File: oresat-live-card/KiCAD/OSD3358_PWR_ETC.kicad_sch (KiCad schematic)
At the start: 35 parts, among them Q1 MMBT2907, U10 TLVH431, U18 RCLAMP0504FB, U4 SN74LVC1G07DCK, U7 OSD3358-512M-BSM

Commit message: Updated OreSat Live Card. Added changes from the C3 v6 Octavo circuitry and GPS card update. Fixed some GitHub issues. Board layout still in progress.
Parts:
- removed C41: 100n, Resistor_SMD:R_0603_1608Metric, symbol Device:C_Small
- removed JP101, JP104: JUMPER-SMT_2_NC_TRACE_SILK, Jumper:SolderJumper-2_P1.3mm_Bridged_RoundedPad1.0x1.5mm, symbol oresat-live-card-eagle-import:JUMPER-SMT_2_NC_TRACE_SILK
- removed R73, R74, R75: 100, Resistor_SMD:R_0603_1608Metric, symbol oresat-live-card-eagle-import:R-US_0603-A
- removed U18: RCLAMP0504FB, oresat-live-card:SC70-6, symbol oresat-live-card-eagle-import:RCLAMP0504FB
- added C33: 100n, Capacitor_SMD:C_0603_1608Metric, symbol Device:C_Small
- added D9 (x2): MBR0520L, Diode_SMD:D_SOD-123, symbol Device:D_Small
- added R48: 10k, Resistor_SMD:R_0603_1608Metric, symbol Device:R_Small_US
- D1: symbol oresat-live-card-eagle-import:LED-GREEN0603 -> Device:LED
- Q1: symbol oresat-live-card-eagle-import:MMBT2907SMD -> Device:Q_PNP_BEC
- R1: value 4.7k -> 10k; symbol oresat-live-card-eagle-import:R-US_0603-A -> oresat-passives:R-US
- R15, R23, R28, R31: symbol oresat-live-card-eagle-import:R-US_0603-A -> oresat-passives:R-US
- TP109, TP110, TP112, TP129, TP130, TP14, TP151, TP155, TP164, TP165, TP2, TP25, TP3, TP4, TP9: footprint oresat-live-card:PAD.03X.04 -> oresat-misc:TestPoint_Pad_D1.0mm; symbol oresat-live-card-eagle-import:TEST-POINT -> oresat-misc:Test-Point-1mm-round
- U10: symbol oresat-live-card-eagle-import:TLVH431 -> oresat-ics:TLVH431
- U4: symbol oresat-live-card-eagle-import:SN74LVC1G07DCK -> oresat-ics:SN74LVC1G07DCK
- U7: footprint oresat-live-card:OSD335X-BGA-256 -> oresat-ics:U-Octavo-OSD335X-BGA-256; symbol oresat-live-card-eagle-import:OSD3358-512M-BSM -> oresat-ics:OSD3358-512M-BSM
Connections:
- net 3.3V: now also D9.1 (K), D9.1 (K), R48.2; no longer U7.F6 (SYS_VDD1_3P3V@1), U7.F7 (SYS_VDD1_3P3V@2), U7.G6 (SYS_VDD1_3P3V@3), U7.G7 (SYS_VDD1_3P3V@4)
- net 3.3VA: now also Q1.2 (E), R23.2, R28.2
- net EEPROM_WP: now also U7.M2 (EEPROM_WP)
- net GND: now also D1.1 (K), C33.2; no longer D1.C
- net I2C0_SCL: now also U7.C10 (I2C0_SCL), U7.D10 (PMIC_SCL)
- net I2C0_SDA: now also U7.C11 (I2C0_SDA), U7.D11 (PMIC_SDA)
- net at R23.1, U10.2 (K): now also Q1.1 (B); no longer Q1.B
- net at R31.1, U10.3 (A): now also C18.1, Q1.3 (C), TP14.1, TP164.1, U4.5 (VCC), U7.K11 (SYS_RTC_1P8V@1), U7.L11 (SYS_RTC_1P8V@2); no longer Q1.C
- net at R1.2: now also D1.2 (A); no longer D1.A
- net RESET# renamed nRESET
- net nRESET: now also C33.1, R48.1
- new net: D9.2 (A), U7.F6 (SYS_VDD1_3P3V@1), U7.F7 (SYS_VDD1_3P3V@2), U7.G6 (SYS_VDD1_3P3V@3), U7.G7 (SYS_VDD1_3P3V@4)
- new net VPD: D9.2 (A)
- no-connect marks 12 -> 11
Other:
- note added: "SYS_VOUT is the OR of 5V from the bus and VIN_USB. Imax = 500 mA"
- note removed: "ESD protection clamping diodes for I2C0 lines. This is required because these lines are routed externally so the internal EEPROM can be programmed."
- note removed: "PMIC_PGOOD drives PWRONRSTN and WARMRSTN when the power supplies are ready. Because of different voltage levels, an open-drain buffer is required."
- note removed: "Power Management Buffer powered from SYS_RTC_1P8V"
- note removed: "SYS_VOUT is where system 5V power originates, 500mA max. This will always be 5V as long as VIN_AC or VIN_USB are used at 5V. However, if VIN_BAT is used with non-5V input, this will reflect that voltage. VIN_BAT will probably be used from the oresat power circuit, so we need to prepare for this case. Likewise, right now the only component using 5V is the USB host circuit"
- note removed: "TODO: Does this need to be 3.3VA?"
- moved on the sheet: C18, R1, TP109, TP112, TP151, TP155, TP25

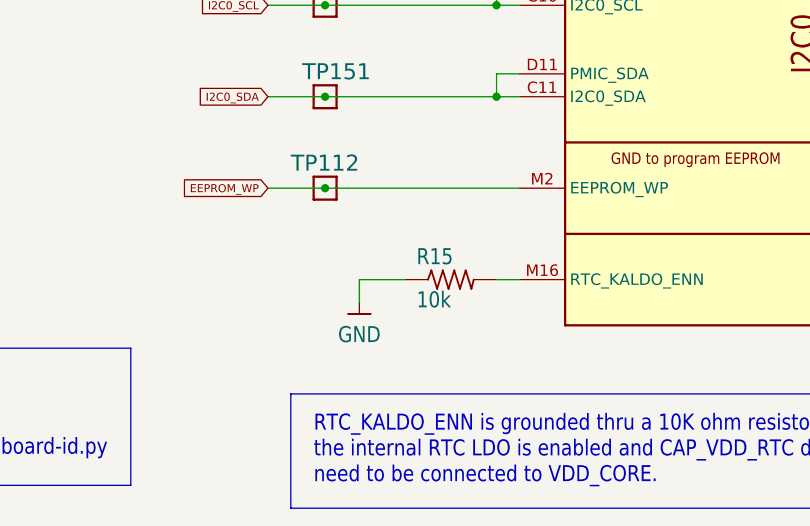
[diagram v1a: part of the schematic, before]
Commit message: Updated silk screen and small schematic changes
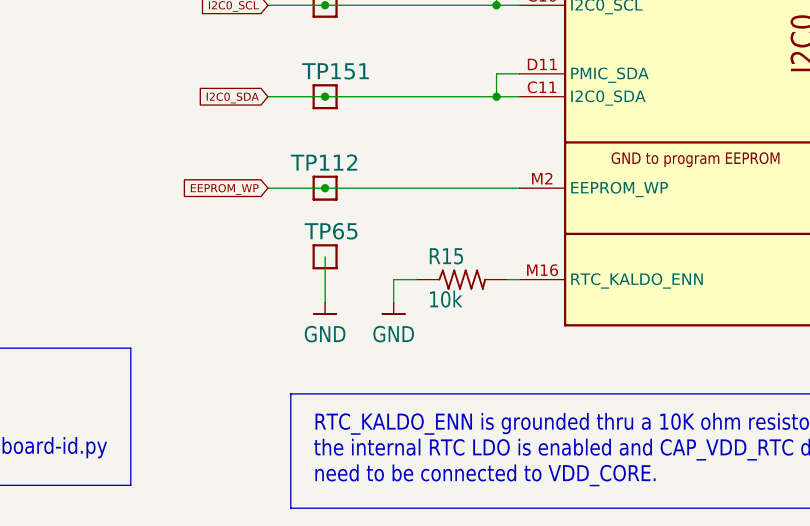
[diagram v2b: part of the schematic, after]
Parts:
- added TP65: TEST-POINT, oresat-misc:TestPoint-0.75mm-th, symbol oresat-misc:Test-Point-1mm-round
- TP112, TP151, TP155: footprint oresat-misc:TestPoint_Pad_D1.0mm -> oresat-misc:TestPoint-0.75mm-th
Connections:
- net GND: now also TP65.1
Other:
- moved on the sheet: R15
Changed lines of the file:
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@@
     (stroke (width 0) (type default))
   )
-  (wire (pts (xy 95.25 223.52) (xy 95.25 226.06))
+  (wire (pts (xy 99.06 223.52) (xy 99.06 226.06))
     (stroke (width 0) (type default))
   )
@@
     (stroke (width 0) (type default))
   )
+  (wire (pts (xy 91.44 220.98) (xy 91.44 226.06))
+    (stroke (width 0) (type default))
+  )
   (wire (pts (xy 398.78 66.04) (xy 393.7 66.04))
     (stroke (width 0) (type default))
@@
     (stroke (width 0) (type default))
   )
-  (wire (pts (xy 113.03 223.52) (xy 110.49 223.52))
+  (wire (pts (xy 113.03 223.52) (xy 111.76 223.52))
     (stroke (width 0) (type default))
   )
@@
     (stroke (width 0) (type default))
   )
-  (wire (pts (xy 100.33 223.52) (xy 95.25 223.52))
+  (wire (pts (xy 101.6 223.52) (xy 99.06 223.52))
     (stroke (width 0) (type default))
   )
@@
     )
   )
-  (symbol (lib_id "oresat-power:GND") (at 95.25 226.06 0) (unit 1)
-    (in_bom yes) (on_board yes) (dnp no)
-    (property "Reference" "#GND069" (at 95.25 226.06 0)
-      (effects (font (size 1.27 1.27)) hide)
-    )
-    (property "Value" "GND" (at 95.25 228.6 0)
+  (symbol (lib_id "oresat-power:GND") (at 99.06 226.06 0) (unit 1)
+    (in_bom yes) (on_board yes) (dnp no)
+    (property "Reference" "#GND069" (at 99.06 226.06 0)
+      (effects (font (size 1.27 1.27)) hide)
+    )
+    (property "Value" "GND" (at 99.06 228.6 0)
       (effects (font (size 1.778 1.5113)) (justify top))
     )
-    (property "Footprint" "oresat-live-card:" (at 95.25 226.06 0)
-      (effects (font (size 1.27 1.27)) hide)
-    )
-    (property "Datasheet" "" (at 95.25 226.06 0)
+    (property "Footprint" "oresat-live-card:" (at 99.06 226.06 0)
+      (effects (font (size 1.27 1.27)) hide)
+    )
+    (property "Datasheet" "" (at 99.06 226.06 0)
       (effects (font (size 1.27 1.27)) hide)
     )
@@
       (effects (font (size 1.778 1.778)) (justify left bottom) hide)
     )
-    (property "Footprint" "oresat-misc:TestPoint_Pad_D1.0mm" (at 81.28 203.2 0)
+    (property "Footprint" "oresat-misc:TestPoint-0.75mm-th" (at 81.28 203.2 0)
       (effects (font (size 1.27 1.27)) hide)
     )
@@
     )
   )
-  (symbol (lib_id "oresat-passives:R-US") (at 105.41 223.52 0) (unit 1)
-    (in_bom yes) (on_board yes) (dnp no)
-    (property "Reference" "R15" (at 101.6 222.0214 0)
+  (symbol (lib_id "oresat-passives:R-US") (at 106.68 223.52 0) (unit 1)
+    (in_bom yes) (on_board yes) (dnp no)
+    (property "Reference" "R15" (at 102.87 222.0214 0)
       (effects (font (size 1.778 1.5113)) (justify left bottom))
     )
-    (property "Value" "10k" (at 101.6 226.822 0)
+    (property "Value" "10k" (at 102.87 226.822 0)
       (effects (font (size 1.778 1.5113)) (justify left bottom))
     )
-    (property "Footprint" "Resistor_SMD:R_0603_1608Metric" (at 105.41 223.52 0)
-      (effects (font (size 1.27 1.27)) hide)
-    )
-    (property "Datasheet" "" (at 105.41 223.52 0)
-      (effects (font (size 1.27 1.27)) hide)
-    )
-    (property "Description" "RES SMD 10K OHM 1% 1/10W 0603" (at 105.41 223.52 0)
-      (effects (font (size 1.27 1.27)) hide)
-    )
-    (property "Distributor" "DigiKey" (at 105.41 223.52 0)
-      (effects (font (size 1.27 1.27)) hide)
-    )
-    (property "MPN" "ERJ-3EKF1002V" (at 105.41 223.52 0)
+    (property "Footprint" "Resistor_SMD:R_0603_1608Metric" (at 106.68 223.52 0)
+      (effects (font (size 1.27 1.27)) hide)
+    )
+    (property "Datasheet" "" (at 106.68 223.52 0)
+      (effects (font (size 1.27 1.27)) hide)
+    )
+    (property "Description" "RES SMD 10K OHM 1% 1/10W 0603" (at 106.68 223.52 0)
+      (effects (font (size 1.27 1.27)) hide)
+    )
+    (property "Distributor" "DigiKey" (at 106.68 223.52 0)
+      (effects (font (size 1.27 1.27)) hide)
+    )
+    (property "MPN" "ERJ-3EKF1002V" (at 106.68 223.52 0)
       (effects (font (size 1.27 1.27)) hide)
     )
@@
       (effects (font (size 1.778 1.778)) (justify left bottom) hide)
     )
-    (property "Footprint" "oresat-misc:TestPoint_Pad_D1.0mm" (at 81.28 193.04 0)
+    (property "Footprint" "oresat-misc:TestPoint-0.75mm-th" (at 81.28 193.04 0)
       (effects (font (size 1.27 1.27)) hide)
     )
@@
       (effects (font (size 1.778 1.778)) (justify left bottom) hide)
     )
-    (property "Footprint" "oresat-misc:TestPoint_Pad_D1.0mm" (at 81.28 213.36 0)
+    (property "Footprint" "oresat-misc:TestPoint-0.75mm-th" (at 81.28 213.36 0)
       (effects (font (size 1.27 1.27)) hide)
     )
@@
     )
   )
+  (symbol (lib_id "oresat-power:GND") (at 91.44 226.06 0) (unit 1)
+    (in_bom yes) (on_board yes) (dnp no)
+    (property "Reference" "#GND052" (at 91.44 226.06 0)
+      (effects (font (size 1.27 1.27)) hide)
+    )
+    (property "Value" "GND" (at 91.44 228.6 0)
+      (effects (font (size 1.778 1.5113)) (justify top))
+    )
+    (property "Footprint" "oresat-live-card:" (at 91.44 226.06 0)
+      (effects (font (size 1.27 1.27)) hide)
+    )
+    (property "Datasheet" "" (at 91.44 226.06 0)
+      (effects (font (size 1.27 1.27)) hide)
+    )
+    (pin "1")
+    (instances
+      (project "oresat-live-card"
+        (path "/748bdd2d-da0a-4240-ba60-0bf881d2ec56/7c9c8fbf-83c8-4463-803c-a3967b810f93"
+          (reference "#GND052") (unit 1)
+        )
+      )
+    )
+  )
   (symbol (lib_id "oresat-misc:Test-Point-1mm-round") (at 194.31 127 90) (unit 1)
     (in_bom yes) (on_board yes) (dnp no)
@@
         )
       )
+    )
+  )
+  (symbol (lib_id "oresat-misc:Test-Point-1mm-round") (at 91.44 220.98 90) (unit 1)
+    (in_bom yes) (on_board yes) (dnp no)
+    (property "Reference" "TP65" (at 95.25 217.17 90)
+      (effects (font (size 1.778 1.778)) (justify left bottom))
+    )
+    (property "Value" "TEST-POINT" (at 93.98 223.52 0)
+      (effects (font (size 1.778 1.778)) (justify left bottom) hide)
+    )
+    (property "Footprint" "oresat-misc:TestPoint-0.75mm-th" (at 81.28 220.98 0)
+      (effects (font (size 1.27 1.27)) hide)
+    )
+    (property "Datasheet" "" (at 91.44 220.98 0)
+      (effects (font (size 1.27 1.27)) hide)
+    )
+    (pin "1")
+    (instances
+      (project "oresat-live-card"
+        (path "/748bdd2d-da0a-4240-ba60-0bf881d2ec56/7c9c8fbf-83c8-4463-803c-a3967b810f93"
+          (reference "TP65") (unit 1)
+        )
+      )

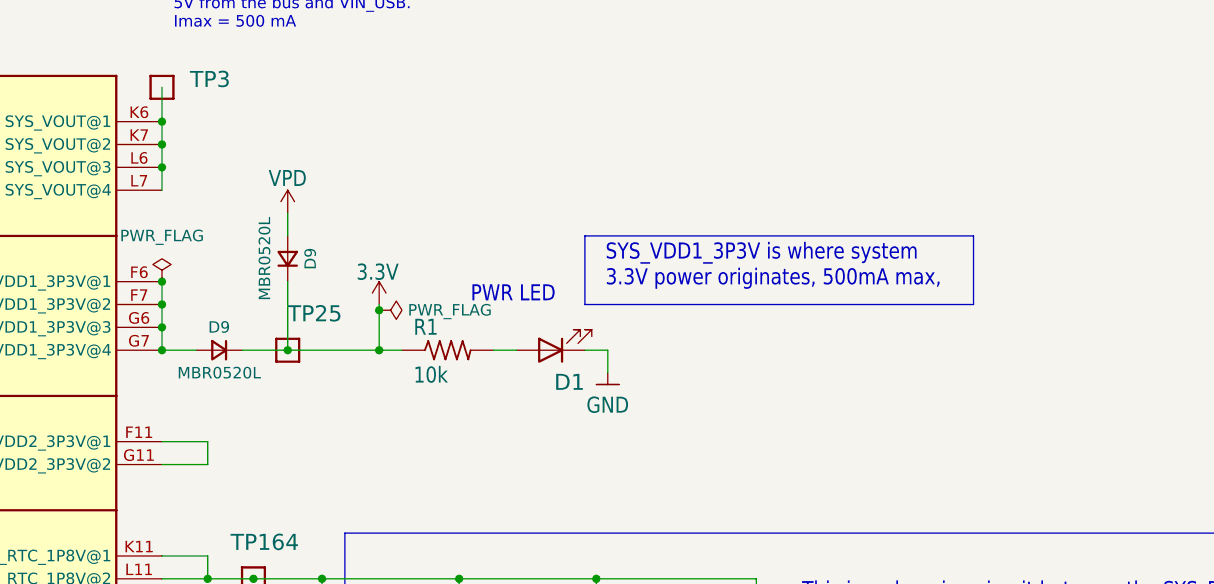
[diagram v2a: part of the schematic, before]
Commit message: Fixed issue with VPD diodes
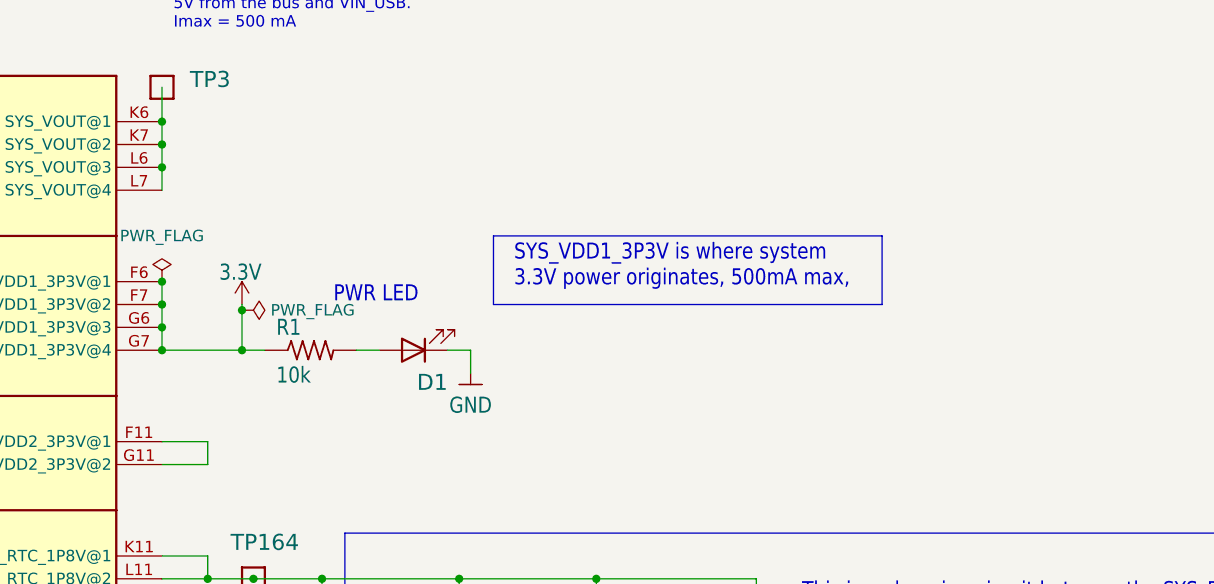
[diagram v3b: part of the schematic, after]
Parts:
- removed D9 (x2): MBR0520L, Diode_SMD:D_SOD-123, symbol Device:D_Small
- removed TP25: TEST-POINT3X4, oresat-misc:TestPoint_Pad_D1.0mm, symbol oresat-misc:Test-Point-1mm-round
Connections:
- net 3.3V: now also U7.F6 (SYS_VDD1_3P3V@1), U7.F7 (SYS_VDD1_3P3V@2), U7.G6 (SYS_VDD1_3P3V@3), U7.G7 (SYS_VDD1_3P3V@4)
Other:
- moved on the sheet: D1, R1

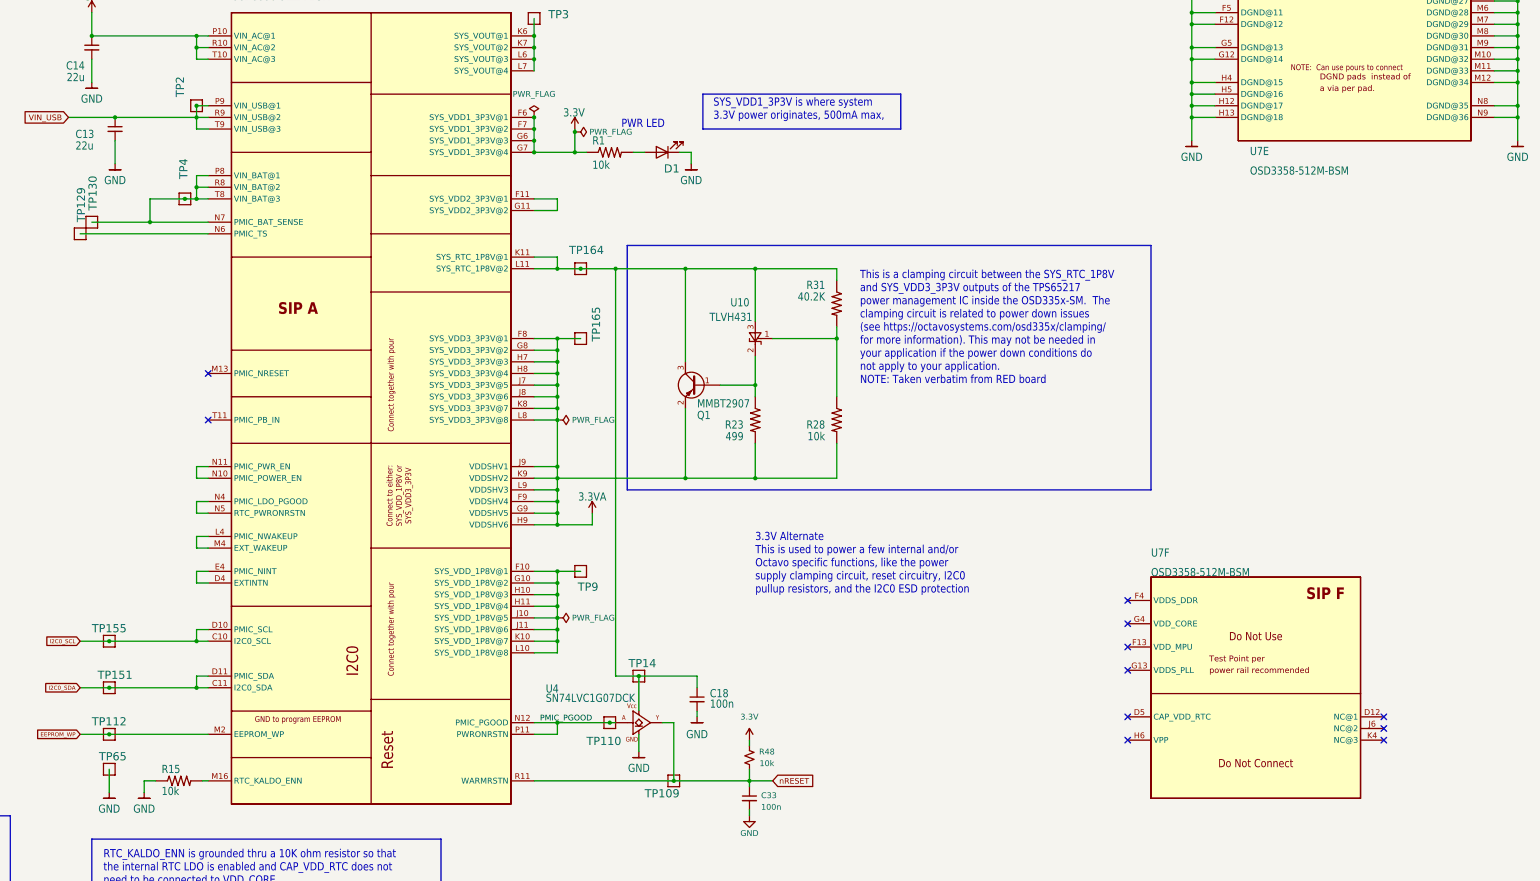
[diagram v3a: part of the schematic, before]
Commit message: Cleaned up ERC and DRC errors on DxWiFi Card
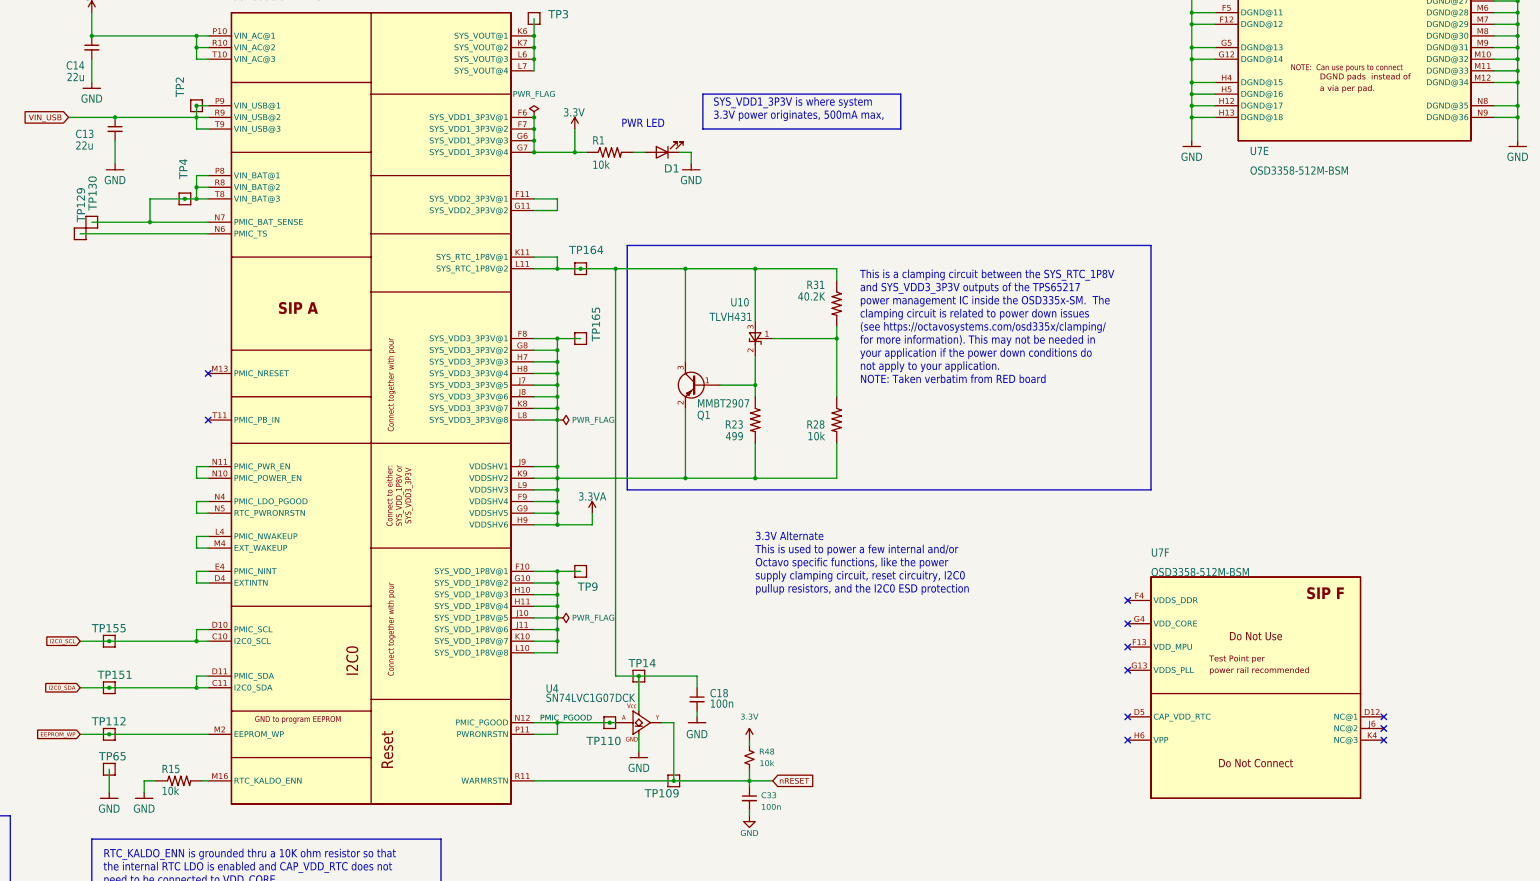
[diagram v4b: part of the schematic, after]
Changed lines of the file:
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@@
   (junction (at 327.66 50.8) (diameter 0) (color 0 0 0 0)
-  )
-  (junction (at 193.04 81.915) (diameter 0) (color 0 0 0 0)
   )
   (junction (at 398.78 68.58) (diameter 0) (color 0 0 0 0)
@@
     (stroke (width 0) (type default))
   )
-  (wire (pts (xy 193.04 81.28) (xy 193.04 81.915))
-    (stroke (width 0) (type default))
-  )
   (wire (pts (xy 85.09 104.14) (xy 113.03 104.14))
     (stroke (width 0) (type default))
@@
     (stroke (width 0) (type default))
   )
-  (wire (pts (xy 193.04 81.915) (xy 193.04 86.36))
+  (wire (pts (xy 193.04 81.28) (xy 193.04 86.36))
     (stroke (width 0) (type default))
   )
@@
         )
       )
-    )
-  )
-  (symbol (lib_id "power:PWR_FLAG") (at 193.04 81.915 270) (unit 1)
-    (in_bom yes) (on_board yes) (dnp no) (fields_autoplaced)
-    (property "Reference" "#FLG02" (at 194.945 81.915 0)
-      (effects (font (size 1.27 1.27)) hide)
-    )
-    (property "Value" "PWR_FLAG" (at 196.215 81.915 90)
-      (effects (font (size 1.27 1.27)) (justify left))
-    )
-    (property "Footprint" "" (at 193.04 81.915 0)
-      (effects (font (size 1.27 1.27)) hide)
-    )
-    (property "Datasheet" "~" (at 193.04 81.915 0)
-      (effects (font (size 1.27 1.27)) hide)
-    )
-    (pin "1")
-    (instances
-      (project "oresat-gps-card"
-        (path "/65d12cdd-c326-4033-9053-c59fa4e0b25e/b9a61b98-fba0-4063-a603-e7fc9d7070a0"
-          (reference "#FLG02") (unit 1)
-        )
-      )
-      (project "oresat-live-card"
-        (path "/748bdd2d-da0a-4240-ba60-0bf881d2ec56/1bdb8d5b-8060-49dd-b753-8985e7684076"
-          (reference "#FLG01") (unit 1)
-        )
-        (path "/748bdd2d-da0a-4240-ba60-0bf881d2ec56/7c9c8fbf-83c8-4463-803c-a3967b810f93"
-          (reference "#FLG05") (unit 1)
-        )
-      )
